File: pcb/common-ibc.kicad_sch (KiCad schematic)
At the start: 86 parts, among them J1 XILINX_JTAG, J10 U.FL, J11 MOLEX_0039291087, J2 MOLEX_0039291067, J3 GROUND, J4 GROUND, J5 MOLEX_0532610571, J6 U.FL, J7 U.FL, J8 U.FL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

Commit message: Most of the way done with layout
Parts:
- removed U1: STM32L431-QFN32, azonenberg_pcb:QFN_32_0.5MM_5x5MM, symbol st-azonenberg:STM32L431-QFN32
- added C25, C26: 0.47 uF, azonenberg_pcb:EIA_0402_CAP_NOSILK, symbol device:C
- added D5: CUHZ16V,H3F, azonenberg_pcb:SOD323H, symbol device:D_Zener
- added FB3: MI0603J601R-10, azonenberg_pcb:EIA_0603_INDUCTOR_NOSILK, symbol passive-azonenberg:INDUCTOR_PWROUT
- added R26, R31: 10K, azonenberg_pcb:EIA_0402_RES_NOSILK, symbol device:R
- added R32: 1K, azonenberg_pcb:EIA_0402_RES_NOSILK, symbol device:R
- added U10: 74LVC1G08, azonenberg_pcb:DFN_6_0.5MM_1.4x1.00MM_NXP_X2-DFN1410-6, symbol special-azonenberg:74LVC1G08
- added U9: STM32L431-QFN48, azonenberg_pcb:QFN_48_0.5MM_7x7MM, symbol st-azonenberg:STM32L431-QFN48
- C21: value 4.7 uF 60V -> 4.7 uF 100V; footprint (none) -> azonenberg_pcb:CAP_TDK_CKG57K
- C22, C23: footprint (none) -> azonenberg_pcb:EIA_1812_CAP_NOSILK
- C6, C7: value PCR1J101MCL1GS -> EEH-ZU1J101V
- D2: value RED -> GREEN
- D3: value GREEN -> RED
- F2: footprint (none) -> azonenberg_pcb:EIA_1206_FUSE_NOSILK
- R24: footprint (none) -> azonenberg_pcb:EIA_0402_RES_NOSILK
- U6: value NCP45560 -> NCP45560IMNTWG-H
- U8: footprint (none) -> azonenberg_pcb:MODULE_MURATA_MYC0409-NA
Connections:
- net 12V0_OUT_EN: now also U10.2 (B), U9.5 (PH0); no longer U6.2 (EN)
- net 12V0_PGOOD: now also U9.32 (PA11)
- net 12V0_REMOTE_VSENSE: now also U9.10 (PA0)
- net 12V0_VSENSE: now also U9.14 (PA4)
- net 12V_SHUNT_FILT: now also U9.16 (PA6)
- net 3V3_SB: now also C26.1, FB3.2, R26.1, U10.6 (VCC), U9.1 (VBAT), U9.24 (VDD), U9.36 (VDD), U9.48 (VDD)
- net 3V3_SB_PGOOD: now also U9.19 (PB1)
- net 48V0_VSENSE: now also U9.12 (PA2)
- net 48V_SHUNT_FILT: now also U9.11 (PA1)
- net 5V0_SB_PGOOD: now also U9.20 (PB2)
- net BOOT0: now also U9.44 (BOOT0)
- net GND: now also C25.2, C26.2, D5.2 (A), R31.1, R32.2, U10.3 (GND), U9.23 (GND), U9.35 (GND), U9.47 (GND), U9.8 (VSSA), U9.PAD (GND)
- net I2C_SCL: now also U9.26 (PB13)
- net I2C_SDA: now also U9.27 (PB14)
- net JTAG_TCK: now also U9.37 (PA14)
- net JTAG_TDI: now also U9.38 (PA15)
- net JTAG_TMS: now also U9.34 (PA13)
- net JTAG_TRST: now also U9.40 (PB4)
- net LED0: now also U9.25 (PB12)
- net LED1: now also U9.28 (PB15)
- net LED2: now also U9.29 (PA8)
- net LOAD_PGOOD: now also U9.22 (PB11)
- net RST_N: now also U9.7 (NRST)
- net TEMP_ALERT: now also R26.2, U9.33 (PA12)
- net UART_RX: now also U9.31 (PA10)
- net UART_TX: now also U9.30 (PA9)
- net at R7.2: now also U9.39 (PB3)
- net 12V0_OUT: now reaches F2.2, J11.1 (P1), J11.2 (P2), J11.3 (P3)
- net 12V0_OUT: now also D5.1 (K)
- new net 12V0_LOAD_EN: R32.1, U10.4 (Y), U6.2 (EN), U9.43 (PB7)
- new net 12V0_OE: R31.2, U10.1 (A), U9.46 (PB9)
- new net A3V3: C25.1, FB3.1, U9.9 (VDDA)
- no-connect marks 10 -> 20
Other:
- note added: "Disable output if interlock trips"
- company: (none) -> Antikernel Labs
- title: (none) -> 48 -> 12V IBC 6A 72W
- moved on the sheet: C1, C15, C16, C17, C2, C21, C22, C23, C3, C4, C5, F2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

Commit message: Finished initial layout of IBC, ready for final review
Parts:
- added Q1: SI7942DP, azonenberg_pcb:SOIC_8_3.9MM, symbol special-azonenberg:SI7942DP_DUAL_NMOS
- added R27: 576K, azonenberg_pcb:EIA_0402_RES_NOSILK, symbol device:R
- added R28, R33: 10M, azonenberg_pcb:EIA_0402_RES_NOSILK, symbol device:R
- added R29: 49.9K, azonenberg_pcb:EIA_0402_RES_NOSILK, symbol device:R
- added R30: 187K, azonenberg_pcb:EIA_0402_RES_NOSILK, symbol device:R
- added R34: 23.2K, azonenberg_pcb:EIA_0402_RES_NOSILK, symbol device:R
- added TP2: TESTPOINT, azonenberg_pcb:TESTPOINT_SMT_0.5MM, symbol conn:CONN_01X01
- added U1: LTC4367, azonenberg_pcb:DFN_8_0.5MM_3x3MM, symbol analog-azonenberg:LTC4367
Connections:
- net 12V0: no longer C18.1, U7.1 (EN), U7.2 (VIN)
- net 12V0_OE: now also U9.21 (PB10); no longer U9.46 (PB9)
- net 12V0_SWIN: now also C18.1, U7.1 (EN), U7.2 (VIN)
- net 12V_SHUNT_FILT: now also U9.17 (PA7); no longer U9.16 (PA6)
- net 3V3_SB_PGOOD: now also U9.13 (PA3); no longer U9.19 (PB1)
- net 48V_CMC: now also Q1.5 (D), Q1.6 (D), R27.1, U1.1 (VIN); no longer FB1.2
- net GND: now also MH1.1 (P1), MH2.1 (P1), MH3.1 (P1), MH4.1 (P1), R30.2, U1.4 (GND), U1.PAD (GND)
- new net: R29.1, R33.2, U1.2 (UV)
- new net: R29.2, R34.1
- new net: R27.2, R28.1, U1.5 (~{SHDN})
- new net: R30.1, R34.2, U1.3 (OV)
- new net: R28.2, R33.1
- new net 48V0_MIDPROT: Q1.1 (S), Q1.3 (S)
- new net 48V_PROT: FB1.2, Q1.7 (D), Q1.8 (D), U1.7 (VOUT)
- new net PROT_FAULT: TP2.1 (P1), U1.6 (~{FAULT})
- new net PROT_GATE: Q1.2 (G), Q1.4 (G), U1.8 (GATE)
- no-connect marks 20 -> 16
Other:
- note added: "Gate output enable from load with software interlock trip flag"
- note added: "Main power converter"
- note added: "R1 -> R30 R2 -> R29+R34 R3 -> R27+R28+R33 Vos 3 mV Ileak 10 nA R1+R2 <= (3 mV / 10 nA) or 300K SHDN: if unused connect to Vin with 510K Must keep below 80V Probably fine to just say 80V is our specced max (almost 2x overvolt) We don't have 510K handy but have 576K so use that Undervoltage trip at 40V R3 = 300K * (40V - 0.5V)/0.5V = 300K * 79 = 23.7M. Too hard to get this value Using 10M for R28/R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"
- note added: "Remote sense is purely for stats and monitoring to detect high contact resistance or a loose power cable. No compensation for output voltage droop is performed."
- note removed: "Disable output if interlock trips"
- note removed: "Remote sense cannot run through load switch but provide monitor feedback through MCU"
- moved on the sheet: C10, C15, C16, C17, C18, C19, C20, C21, C22, C23, C26, C6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

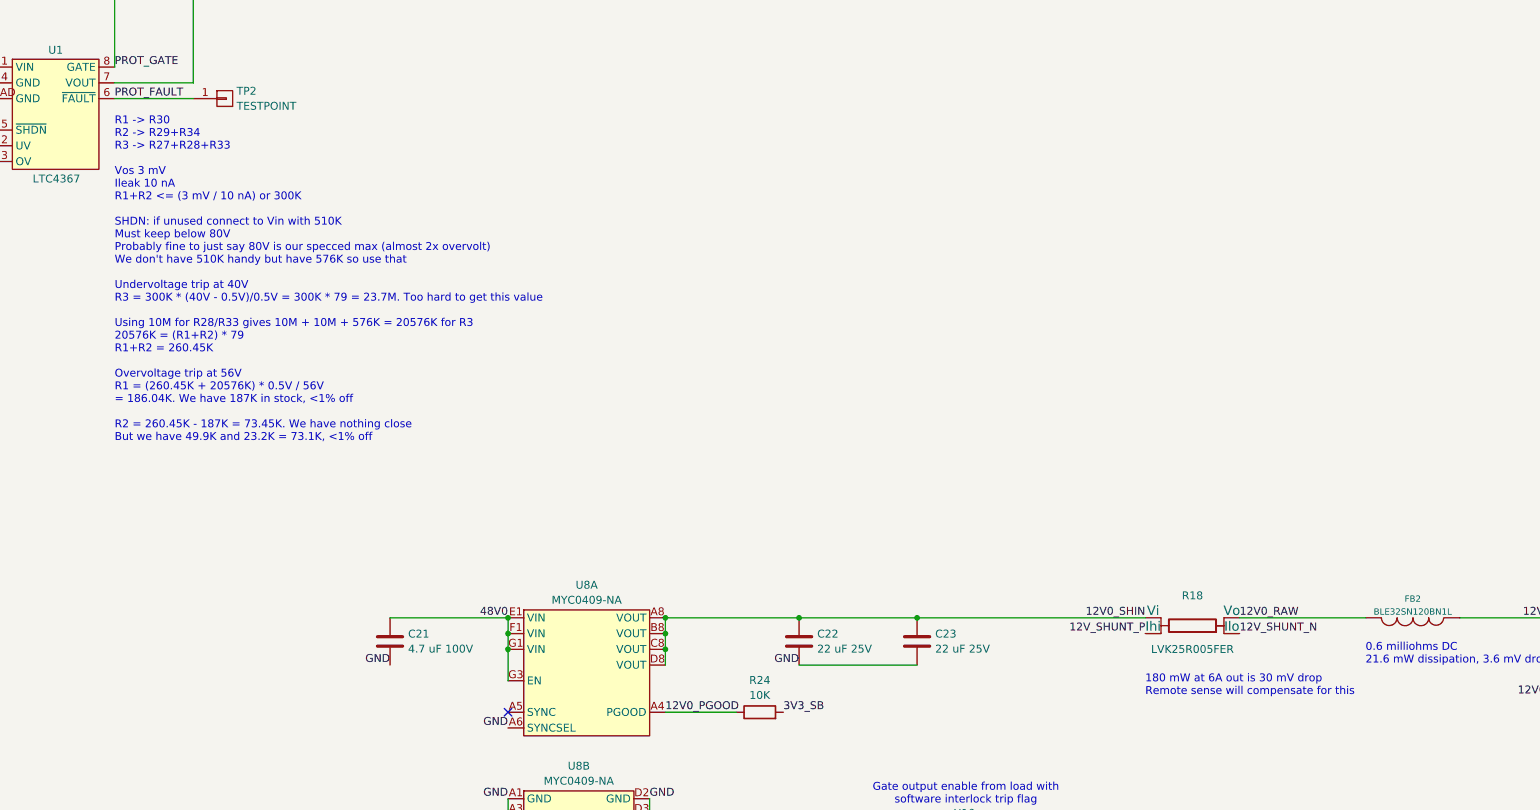
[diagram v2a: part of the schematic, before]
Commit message: Finished layout review on IBC, made some tweaks to routing and solder paste
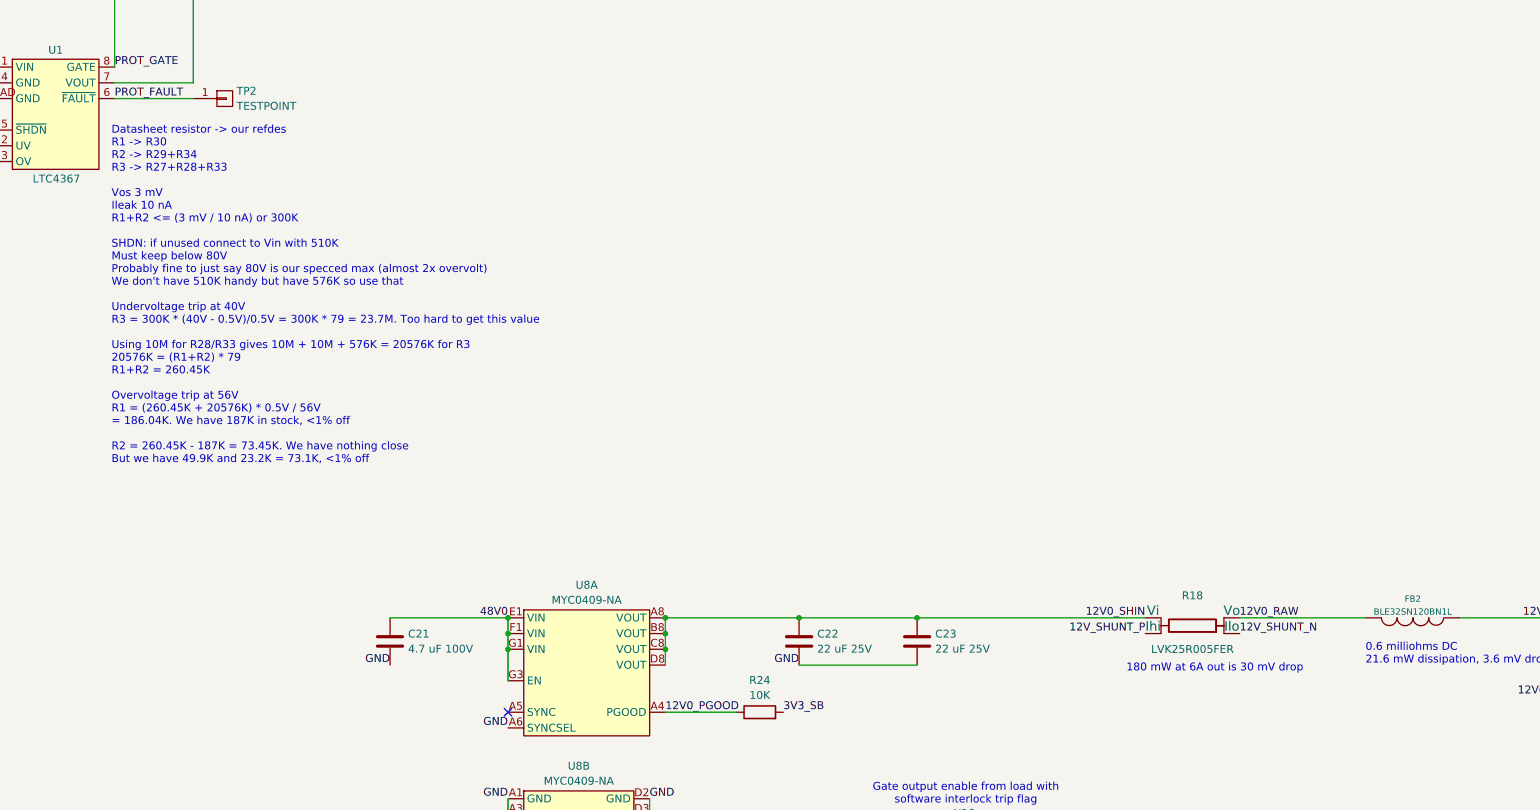
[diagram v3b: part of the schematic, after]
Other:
- note added: "180 mW at 6A out is 30 mV drop"
- note added: "Datasheet resistor -> our refdes R1 -> R30 R2 -> R29+R34 R3 -> R27+R28+R33 Vos 3 mV Ileak 10 nA R1+R2 <= (3 mV / 10 nA) or 300K SHDN: if unused connect to Vin with 510K Must keep below 80V Probably fine to just say 80V is our specced max (almost 2x overvolt) We don't have 510K handy but have 576K so use that Undervoltage trip at 40V R3 = 300K * (40V - 0.5V)/0.5V = 300K * 79 = 23.7M. Too hard to g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"
- note removed: "180 mW at 6A out is 30 mV drop Remote sense will compensate for this"
- note removed: "R1 -> R30 R2 -> R29+R34 R3 -> R27+R28+R33 Vos 3 mV Ileak 10 nA R1+R2 <= (3 mV / 10 nA) or 300K SHDN: if unused connect to Vin with 510K Must keep below 80V Probably fine to just say 80V is our specced max (almost 2x overvolt) We don't have 510K handy but have 576K so use that Undervoltage trip at 40V R3 = 300K * (40V - 0.5V)/0.5V = 300K * 79 = 23.7M. Too hard to get this value Using 10M for R28/R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"
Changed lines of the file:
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@@
 	(title_block
 		(title "48 -> 12V IBC 6A 72W")
-		(date "2024-07-04")
+		(date "2024-07-06")
 		(rev "0.4")
 		(company "Antikernel Labs")
@@
 		)
 	)
-	(text "R1 -> R30\nR2 -> R29+R34\nR3 -> R27+R28+R33\n\nVos 3 mV\nIleak 10 nA\nR1+R2 <= (3 mV / 10 nA) or 300K\n\nSHDN: if unused connect to Vin with 510K\nMust keep below 80V\nProbably fine to just say 80V is our specced max (almost 2x overvolt)\nWe don't have 510K handy but have 576K so use that\n\nUndervoltage trip at 40V\nR3 = 300K * (40V - 0.5V)/0.5V = 300K * 79 = 23.7M. Too hard to get this value\n\nUsing 10M for R28/R33 gives 10M + 10M + 576K = 20576K for R3\n20576K = (R1+R2) * 79\nR1+R2 = 260.45K\n\nOvervoltage trip at 56V\nR1 = (260.45K + 20576K) * 0.5V / 56V \n= 186.04K. We have 187K in stock, <1% off\n\nR2 = 260.45K - 187K = 73.45K. We have nothing close\nBut we have 49.9K and 23.2K = 73.1K, <1% off"
+	(text "Datasheet resistor -> our refdes\nR1 -> R30\nR2 -> R29+R34\nR3 -> R27+R28+R33\n\nVos 3 mV\nIleak 10 nA\nR1+R2 <= (3 mV / 10 nA) or 300K\n\nSHDN: if unused connect to Vin with 510K\nMust keep below 80V\nProbably fine to just say 80V is our specced max (almost 2x overvolt)\nWe don't have 510K handy but have 576K so use that\n\nUndervoltage trip at 40V\nR3 = 300K * (40V - 0.5V)/0.5V = 300K * 79 = 23.7M. Too hard to get this value\n\nUsing 10M for R28/R33 gives 10M + 10M + 576K = 20576K for R3\n20576K = (R1+R2) * 79\nR1+R2 = 260.45K\n\nOvervoltage trip at 56V\nR1 = (260.45K + 20576K) * 0.5V / 56V \n= 186.04K. We have 187K in stock, <1% off\n\nR2 = 260.45K - 187K = 73.45K. We have nothing close\nBut we have 49.9K and 23.2K = 73.1K, <1% off"
 		(exclude_from_sim no)
-		(at 138.43 78.74 0)
+		(at 137.922 81.28 0)
 		(effects
 			(font
@@
 		)
 	)
-	(text "180 mW at 6A out is 30 mV drop\nRemote sense will compensate for this"
+	(text "180 mW at 6A out is 30 mV drop"
 		(exclude_from_sim no)
-		(at 304.8 146.05 0)
+		(at 301.752 142.24 0)
 		(effects
 			(font

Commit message: Initial IBC bootloader
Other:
- note added: "Planned changes: * Inrush limiter in Q1 see datasheet figure 14 * TVS see figure 15"
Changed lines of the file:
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@@
+		)
+	)
+	(text "Planned changes:\n* Inrush limiter in Q1 see datasheet figure 14\n* TVS see figure 15"
+		(exclude_from_sim no)
+		(at 252.984 51.562 0)
+		(effects
+			(font
+				(size 1.27 1.27)
+			)
+			(justify left)
 		)
 	)

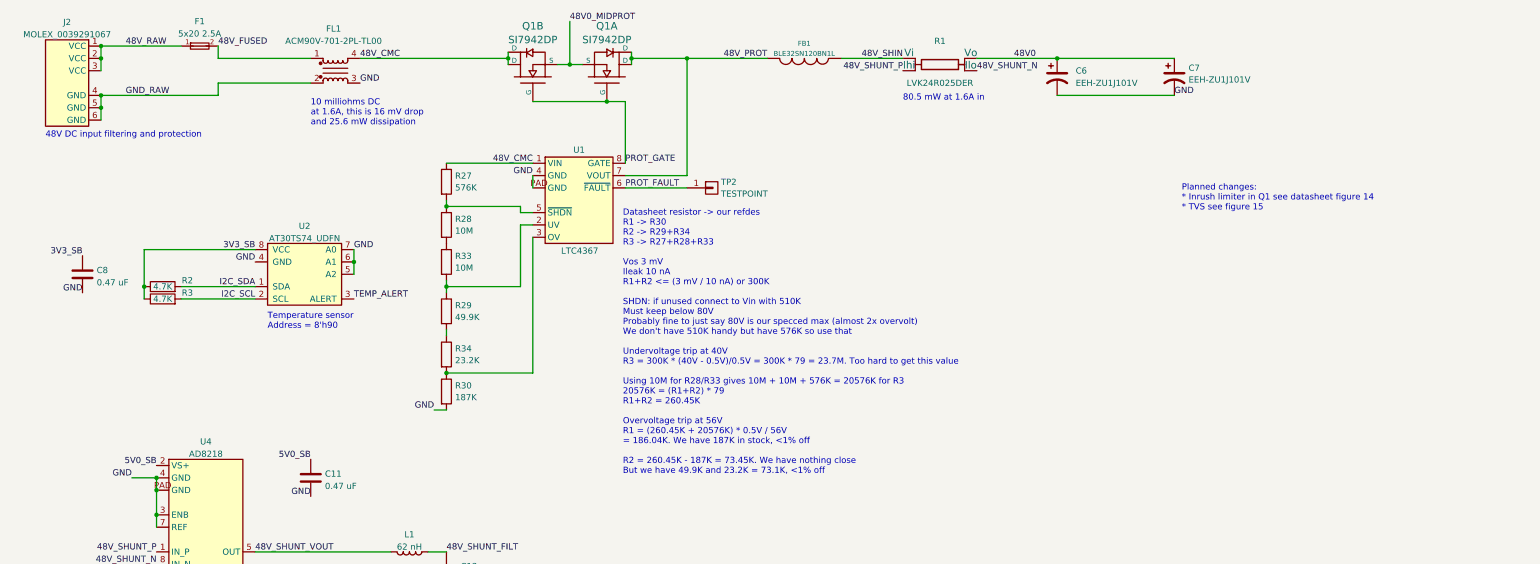
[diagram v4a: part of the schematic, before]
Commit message: Now at minimum functional state with no I2C management support
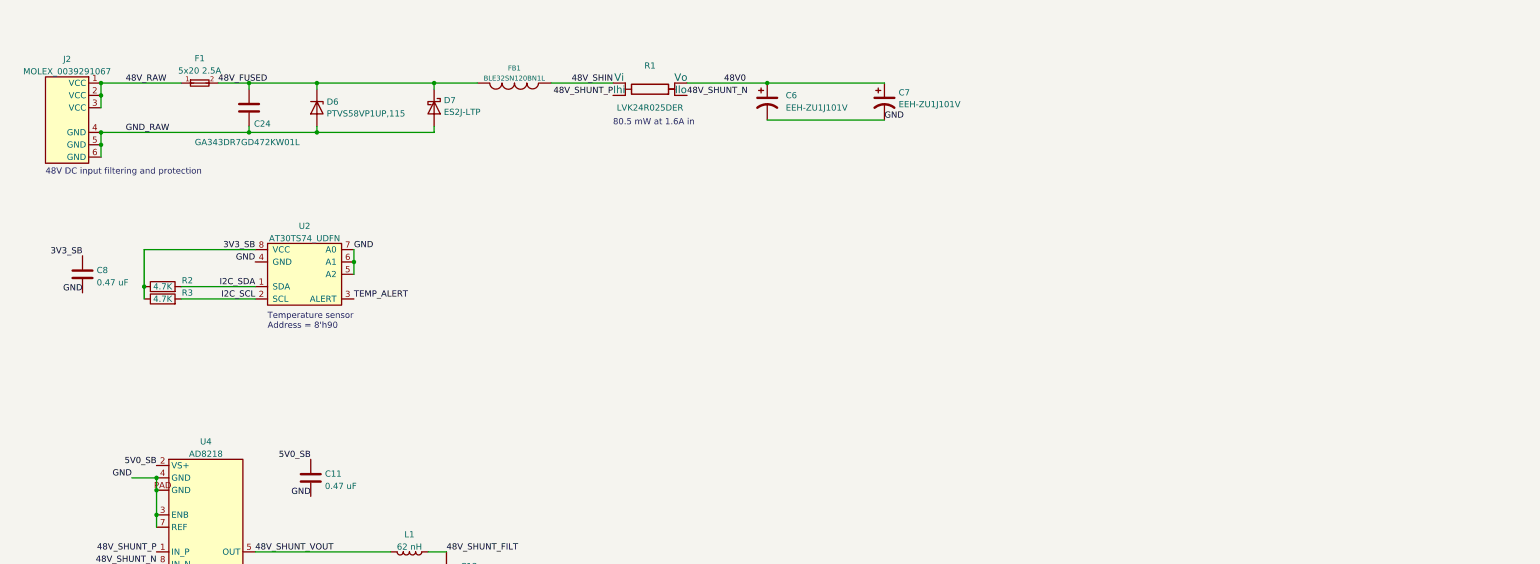
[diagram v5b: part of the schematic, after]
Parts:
- removed FL1: ACM90V-701-2PL-TL00, azonenberg_pcb:CMC_TDK_ACM90V, symbol power-azonenberg:CMC_PowerInOut
- removed Q1: SI7942DP, azonenberg_pcb:SOIC_8_3.9MM, symbol special-azonenberg:SI7942DP_DUAL_NMOS
- removed R27: 576K, azonenberg_pcb:EIA_0402_RES_NOSILK, symbol device:R
- removed R28, R33: 10M, azonenberg_pcb:EIA_0402_RES_NOSILK, symbol device:R
- removed R29: 49.9K, azonenberg_pcb:EIA_0402_RES_NOSILK, symbol device:R
- removed R30: 187K, azonenberg_pcb:EIA_0402_RES_NOSILK, symbol device:R
- removed R34: 23.2K, azonenberg_pcb:EIA_0402_RES_NOSILK, symbol device:R
- removed TP2: TESTPOINT, azonenberg_pcb:TESTPOINT_SMT_0.5MM, symbol conn:CONN_01X01
- removed U1: LTC4367, azonenberg_pcb:DFN_8_0.5MM_3x3MM, symbol analog-azonenberg:LTC4367
- added C24: GA343DR7GD472KW01L, symbol device:C
- added D6: PTVS58VP1UP,115, symbol device:D_Zener
- added D7: ES2J-LTP, symbol device:D_Schottky
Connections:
- net 48V_PROT is gone; now on net 48V_FUSED: FB1.2
- net 48V_FUSED: now also C24.1, D6.1 (K), D7.1 (K)
- net GND_RAW: now also C24.2, D6.2 (A), D7.2 (A)
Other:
- note removed: "10 milliohms DC at 1.6A, this is 16 mV drop and 25.6 mW dissipation"
- note removed: "Datasheet resistor -> our refdes R1 -> R30 R2 -> R29+R34 R3 -> R27+R28+R33 Vos 3 mV Ileak 10 nA R1+R2 <= (3 mV / 10 nA) or 300K SHDN: if unused connect to Vin with 510K Must keep below 80V Probably fine to just say 80V is our specced max (almost 2x overvolt) We don't have 510K handy but have 576K so use that Undervoltage trip at 40V R3 = 300K * (40V - 0.5V)/0.5V = 300K * 79 = 23.7M. Too hard to g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"
- note removed: "Planned changes: * Inrush limiter in Q1 see datasheet figure 14 * TVS see figure 15"
- moved on the sheet: C6, C7, F1, FB1, J2, R1
